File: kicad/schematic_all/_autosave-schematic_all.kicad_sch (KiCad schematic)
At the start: 31 parts, among them J1 Power In, SW1 Button 1, SW2 Encoder 1, SW3 Button 2, SW4 Encoder 2, SW5 Button 3, U2 RPi_Pico, U3 RDA5807M_Module, U4 LM386

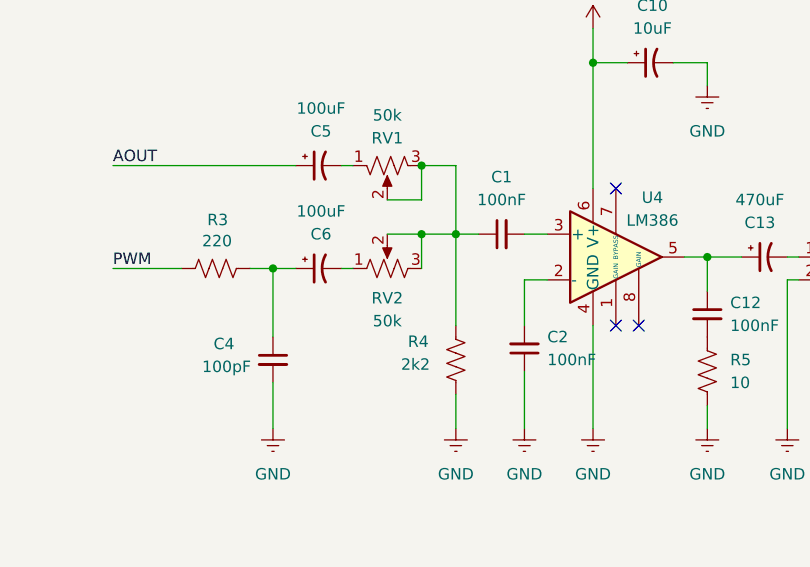
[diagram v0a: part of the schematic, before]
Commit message: Made some minor changes to the schmatic (Changed PWM pin, filtering capacitor footprints and values), and made some progress on the layout & design of the PCB
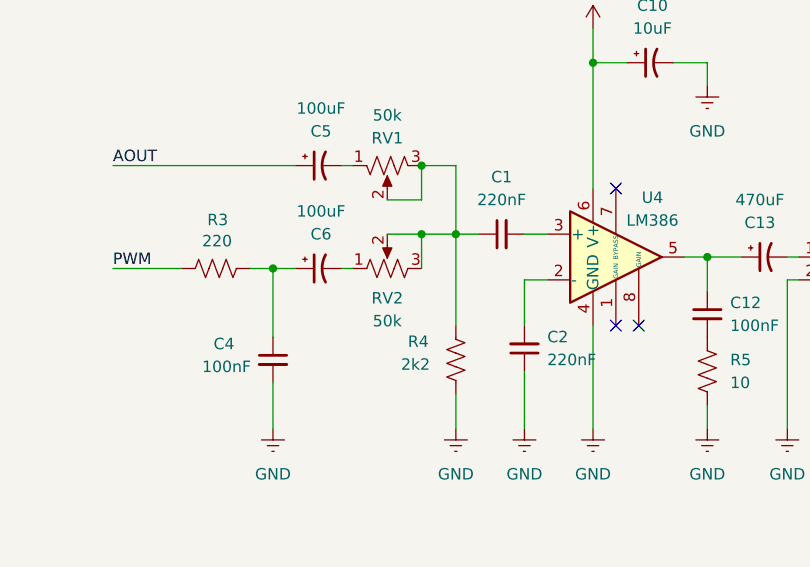
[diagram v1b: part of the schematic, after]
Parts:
- C1, C2: value 100nF -> 220nF
- C4: value 100pF -> 100nF
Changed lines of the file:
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@@
 			)
 		)
-		(property "Value" "100nF"
+		(property "Value" "220nF"
 			(at 228.6063 123.19 90)
 			(effects
@@
 			)
 		)
-		(property "Value" "100nF"
+		(property "Value" "220nF"
 			(at 233.68 140.9635 0)
 			(effects
@@
 			)
 		)
-		(property "Value" "100pF"
+		(property "Value" "100nF"
 			(at 195.326 141.732 0)
 			(effects
